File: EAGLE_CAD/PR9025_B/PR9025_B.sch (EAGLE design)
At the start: 62 parts, among them SW1 C&K_PTS645, U1 SI4702-C19-GMR, X1 ABS25XTAL

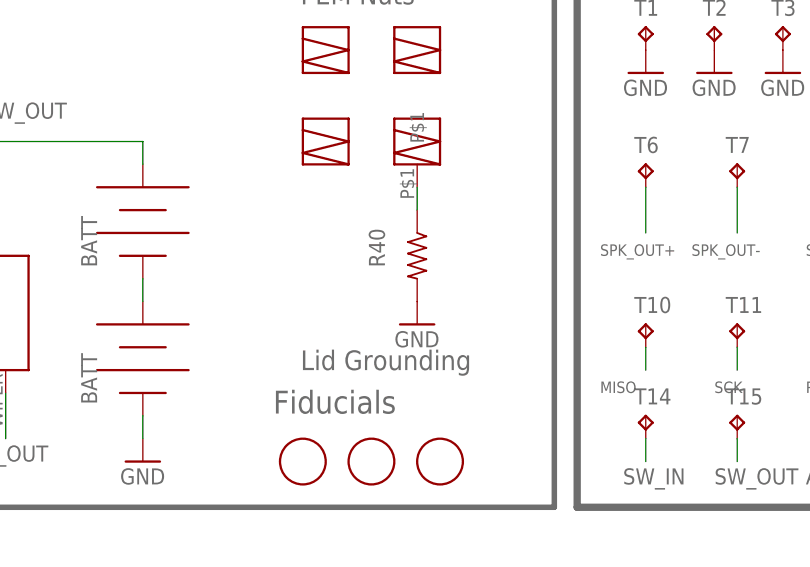
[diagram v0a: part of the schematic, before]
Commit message: PR9025B
Centered ISP header and finished layout.
Moved optimized placement for reverse mount LED
Removed R40 and made a short
Optimized vias placements
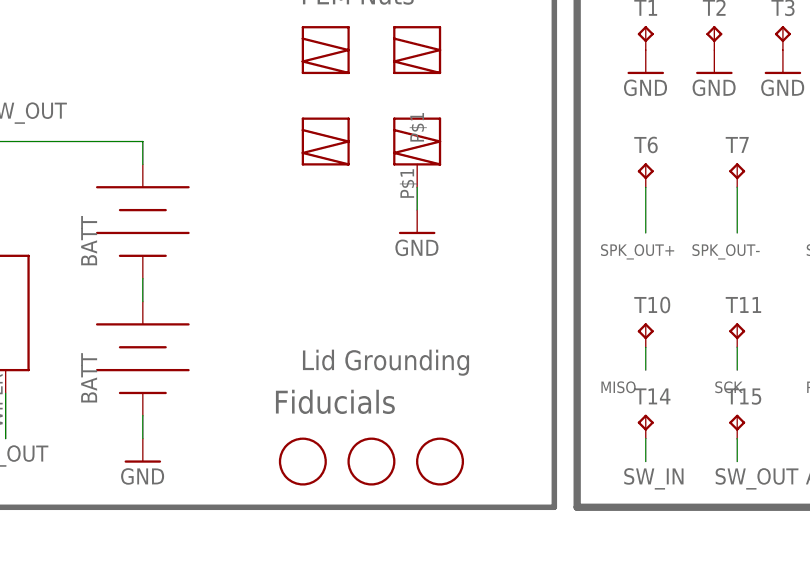
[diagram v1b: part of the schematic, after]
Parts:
- removed R40: DNP, PR_Parts_Library:R_SMT_R0603_CPL
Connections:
- removed net N$6: R40.1, U$5.P$1
- net GND: now also U$5.P$1; no longer R40.2
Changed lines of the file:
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@@
 <attribute name="VOLTAGE" value="16V"/>
-</part>
-<part name="R40" library="PR_Parts_Library" deviceset="R_SMT" device="_R0603_CPL" value="DNP">
-<attribute name="MFG_PN" value="ERJ-3GEY0R00V"/>
 </part>
 <part name="D1" library="PR_Parts_Library" deviceset="BAV99" device="">
@@
 <instance part="GND5" gate="1" x="-20.32" y="99.06"/>
 <instance part="GND2" gate="1" x="-35.56" y="111.76"/>
-<instance part="GND12" gate="1" x="40.64" y="109.22"/>
+<instance part="GND12" gate="1" x="40.64" y="119.38"/>
 <instance part="GND3" gate="1" x="-27.94" y="129.54"/>
 <instance part="MCU" gate="G$1" x="175.26" y="124.46"/>
@@
 <attribute name="NAME" x="177.038" y="20.193" size="1.778" layer="95"/>
 <attribute name="VALUE" x="176.276" y="17.653" size="1.778" layer="96"/>
-</instance>
-<instance part="R40" gate="G$1" x="40.64" y="116.84" smashed="yes" rot="R270">
-<attribute name="NAME" x="37.0586" y="115.57" size="1.778" layer="95" rot="R90"/>
 </instance>
 <instance part="D1" gate="G$1" x="-10.16" y="25.4" rot="R180"/>
@@
 </segment>
 <segment>
+<pinref part="U$5" gate="G$1" pin="P$1"/>
+<wire x1="40.64" y1="121.92" x2="40.64" y2="124.46" width="0.1524" layer="91"/>
 <pinref part="GND12" gate="1" pin="GND"/>
-<pinref part="R40" gate="G$1" pin="2"/>
 </segment>
 </net>
@@
 </segment>
 </net>
-<net name="N$6" class="0">
-<segment>
-<pinref part="U$5" gate="G$1" pin="P$1"/>
-<pinref part="R40" gate="G$1" pin="1"/>
-<wire x1="40.64" y1="121.92" x2="40.64" y2="124.46" width="0.1524" layer="91"/>
-</segment>
-</net>
